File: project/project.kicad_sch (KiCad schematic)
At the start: 41 parts, among them J101 BUS, J102 rs485, J103 qwiic, J104 FFC, J105 Bot, J106 FFC, J107 Top, J108 Mid, J109 Mid, J110 USB_C_Receptacle_USB2.0, J111 BUS, SW101 15mm, SW102 15mm, U101 TMP102, U102 24C02S, U103 USBLC6-2SC6, U104 TMP102, U105 INA226

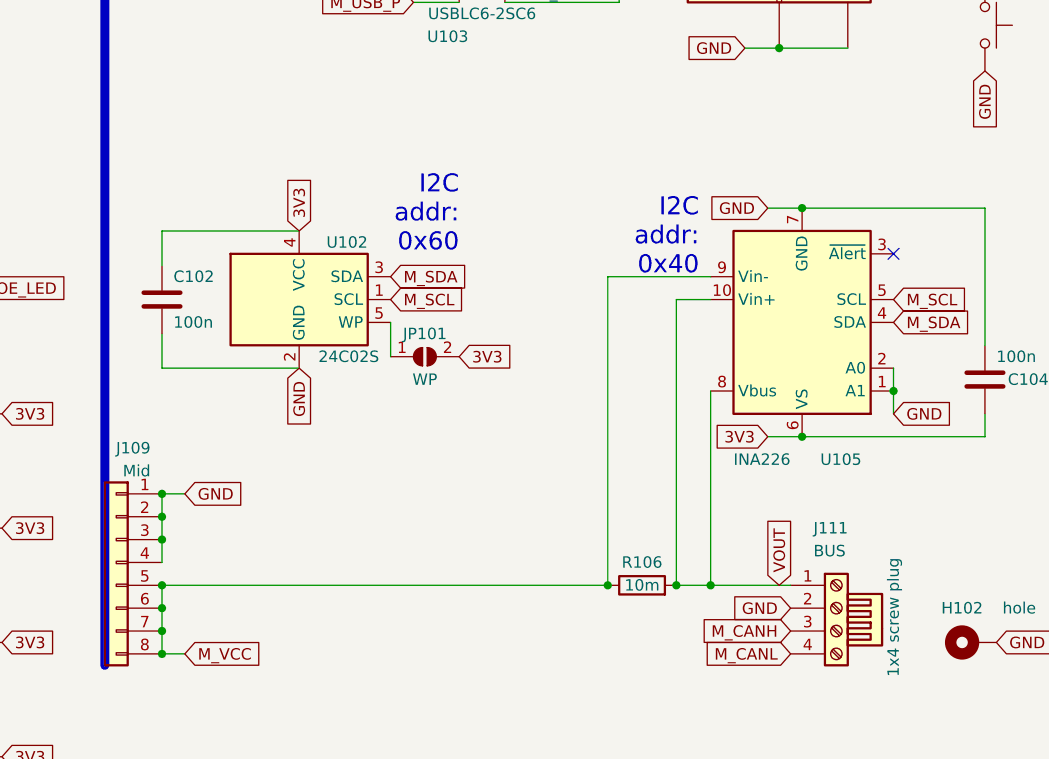
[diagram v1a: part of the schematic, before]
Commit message: adding fuse to power monitor to prevent reverse polarity damage
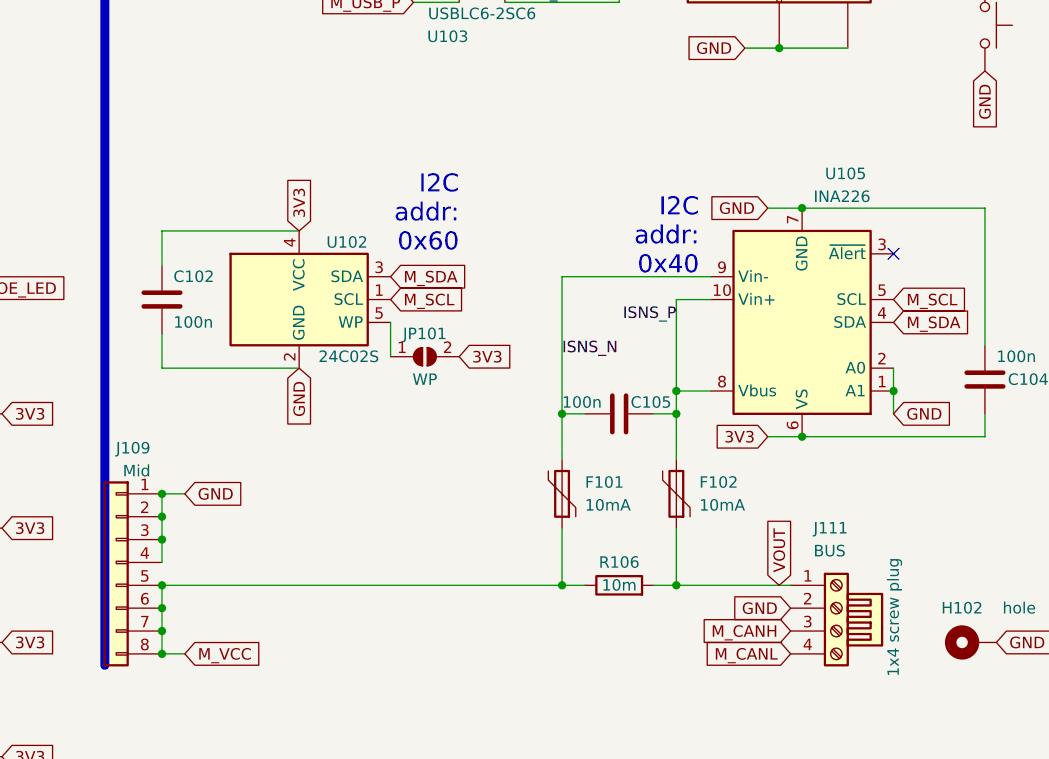
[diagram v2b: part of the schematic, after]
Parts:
- added C105: 100n, Capacitor_SMD:C_0402_1005Metric_Pad0.74x0.62mm_HandSolder, symbol Device:C
- added F101, F102: 10mA, Fuse:Fuse_0805_2012Metric_Pad1.15x1.40mm_HandSolder, symbol Device:Polyfuse
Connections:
- net M_VCC: now also F101.1; no longer U105.9 (Vin-)
- net VOUT: now also F102.1; no longer U105.10 (Vin+), U105.8 (Vbus)
- new net ISNS_N: C105.2, F101.2, U105.9 (Vin-)
- new net ISNS_P: C105.1, F102.2, U105.10 (Vin+), U105.8 (Vbus)
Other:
- moved on the sheet: R106
